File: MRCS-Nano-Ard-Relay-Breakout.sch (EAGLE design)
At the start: 18 parts, among them CON1 5V PWR, J1 5V PWR, J2 Unused I/O, J4 Outputs

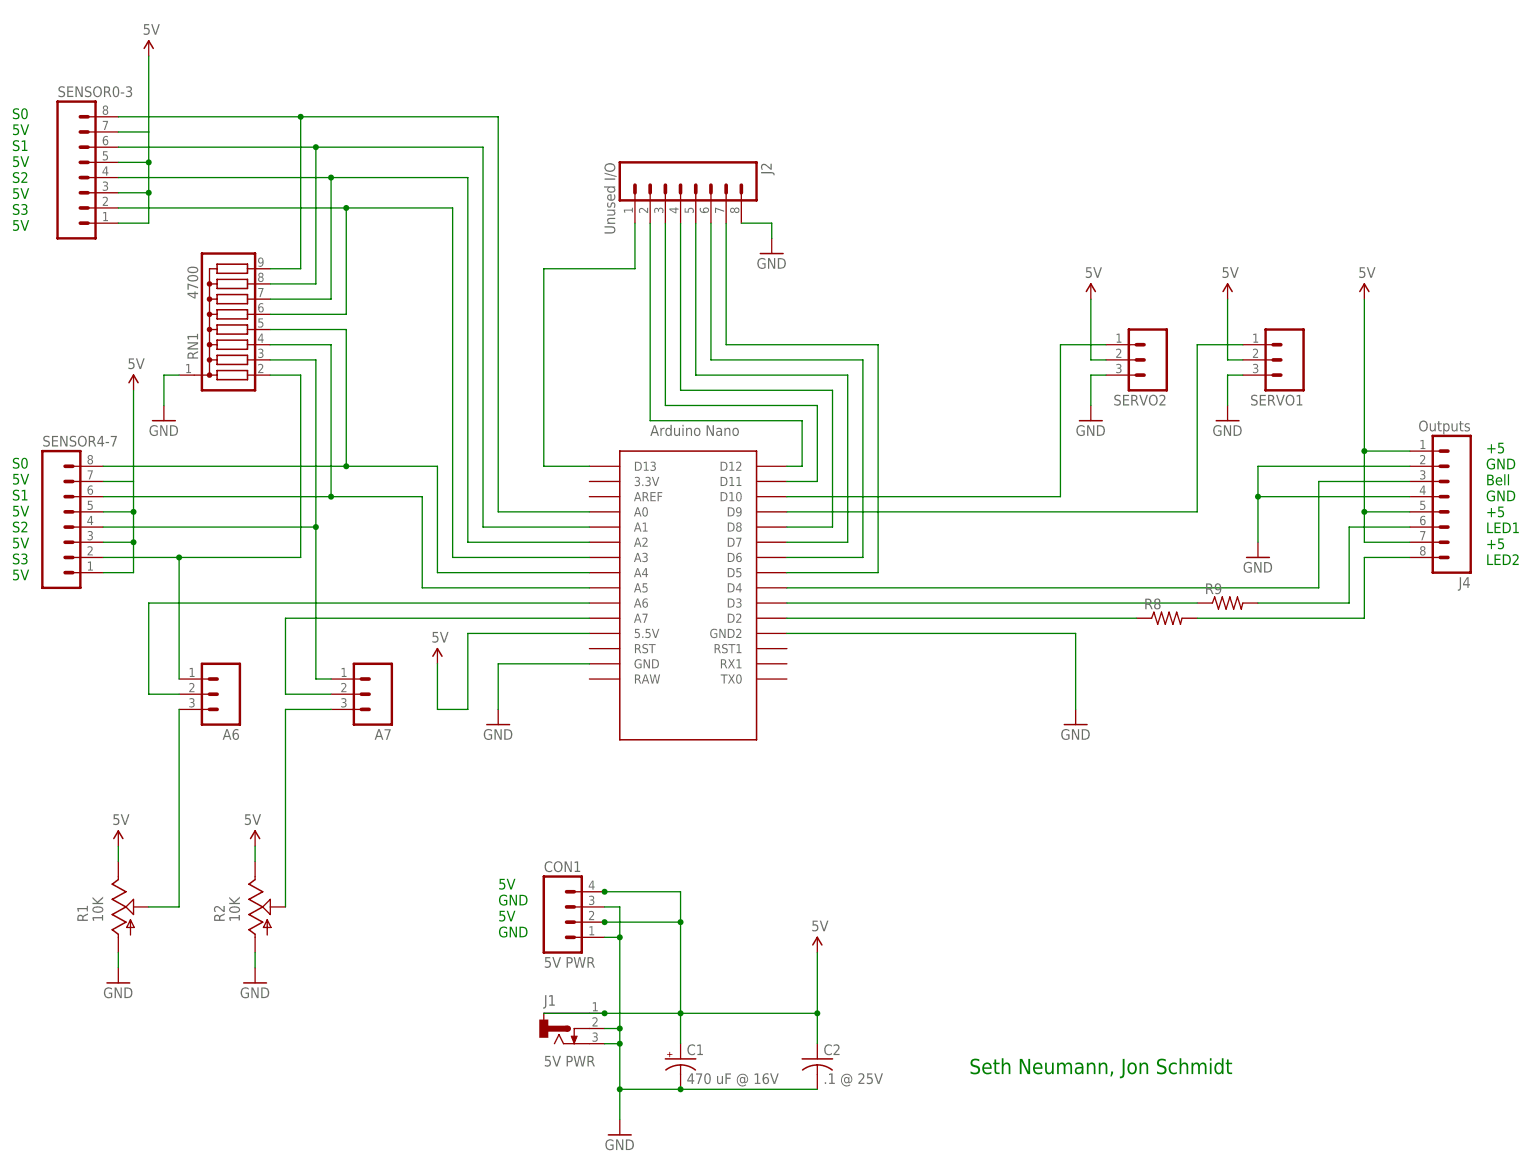
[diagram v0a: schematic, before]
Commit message: minor label changes after design review
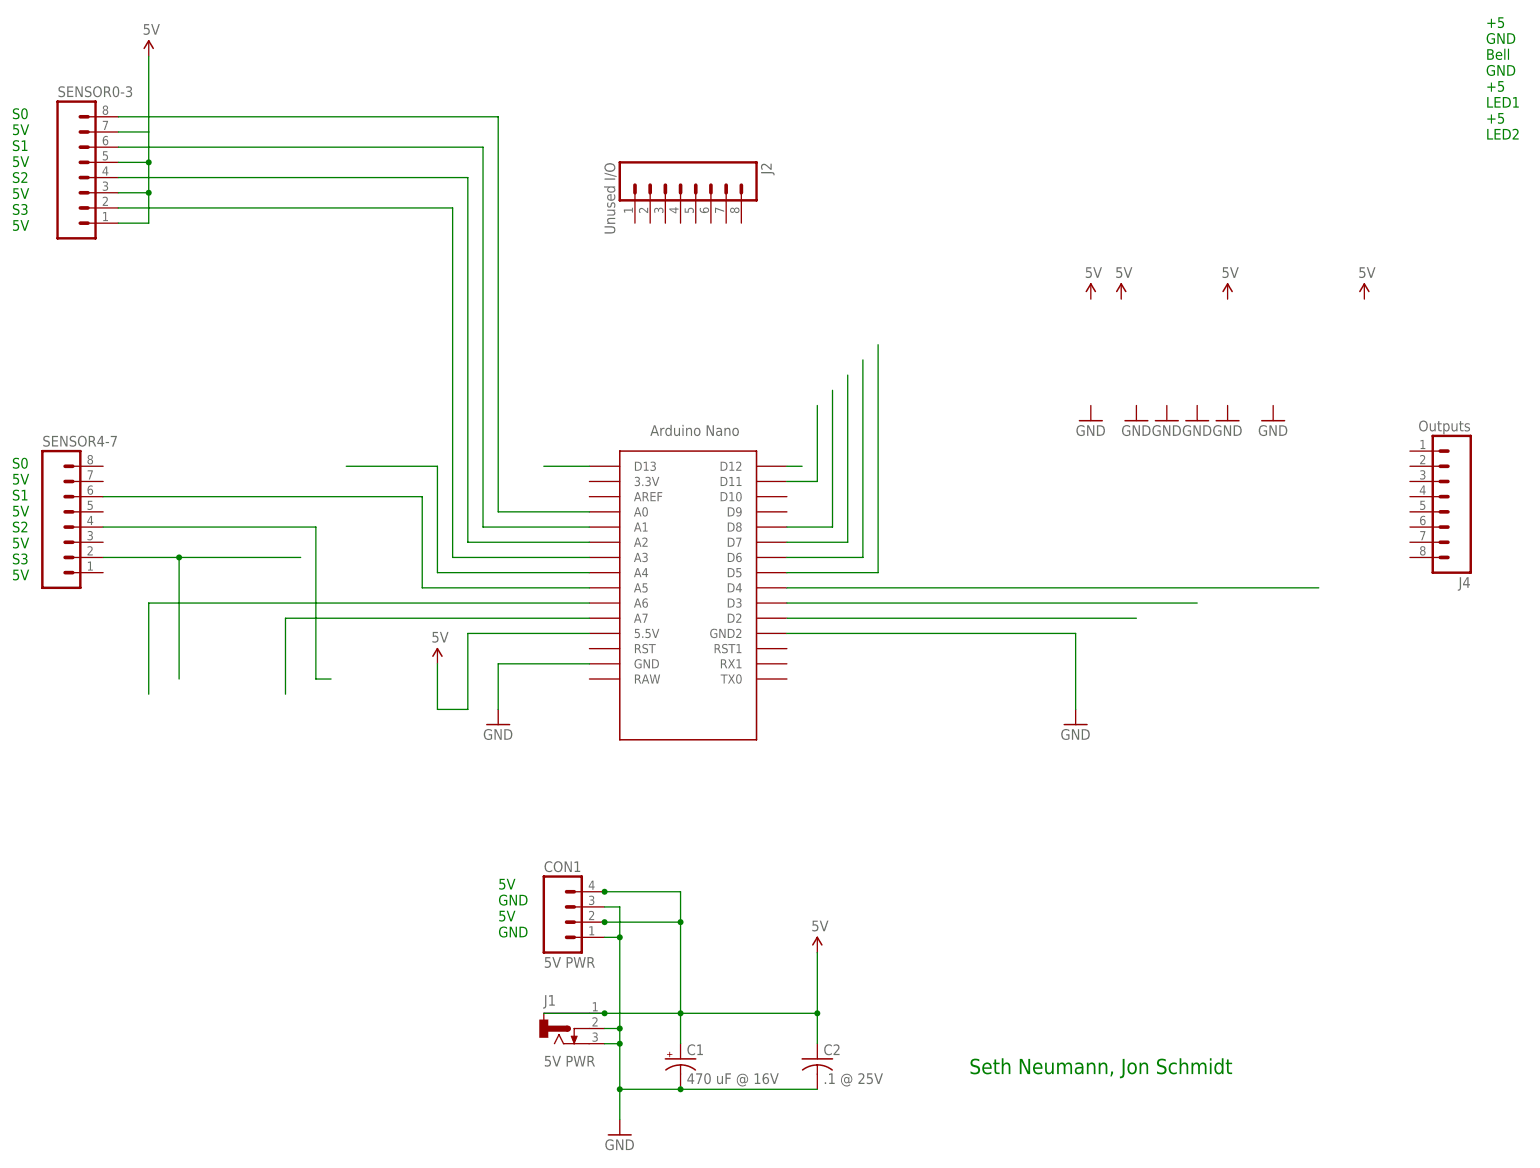
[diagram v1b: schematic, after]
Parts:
- removed A6, A7, SERVO1, SERVO2: (no value), SparkFun-Connectors:M03LOCK
- removed R1, R2: 10K, pot:TRIM_US-RS3
- removed R8, R9: (no value), SPCoast:RPTH-R0
- removed RN1: 4700, resistor-sil:G08R
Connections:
- removed net N$14: A6.3, R1.S
- removed net N$18: A7.3, R2.S
- removed net N$19: J2.1, U$1.D13
- removed net N$5: J4.6, R9.2
- removed net N$8: SERVO2.1, U$1.D10
- removed net N$9: SERVO1.1, U$1.D9
- net 5V: no longer J4.1, J4.5, J4.7, R1.E, R2.E, SENSOR4-7.1, SENSOR4-7.3, SENSOR4-7.5, SENSOR4-7.7, SERVO1.2, SERVO2.2
- net A0: no longer RN1.9
- net GND: no longer J2.8, J4.2, J4.4, R1.A, R2.A, RN1.1, SERVO1.3, SERVO2.3
- net N$1: no longer RN1.5, SENSOR4-7.8
- net N$10: no longer RN1.7
- net N$11: no longer A7.1, RN1.3
- net N$12: no longer RN1.6
- net N$13: no longer A6.1, RN1.2
- net N$15: no longer A6.2
- net N$16: no longer A7.2
- net N$17: no longer RN1.8
- net N$2: no longer R8.1
- net N$20: no longer J2.2
- net N$21: no longer J2.3
- net N$22: no longer J2.4
- net N$23: no longer J2.5
- net N$24: no longer J2.6
- net N$25: no longer J2.7
- net N$3: now also U$1.D13; no longer J4.8, R8.2
- net N$4: no longer R9.1
- net N$6: no longer J4.3
- net N$7: no longer RN1.4
